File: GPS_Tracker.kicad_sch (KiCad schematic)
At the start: 46 parts, among them IC1 SX1278IMLTRT, IC2 PE4259, J8 Antena_Coaxial, Q1 2SC3356-T1B-A_AS, Y2 32MHz

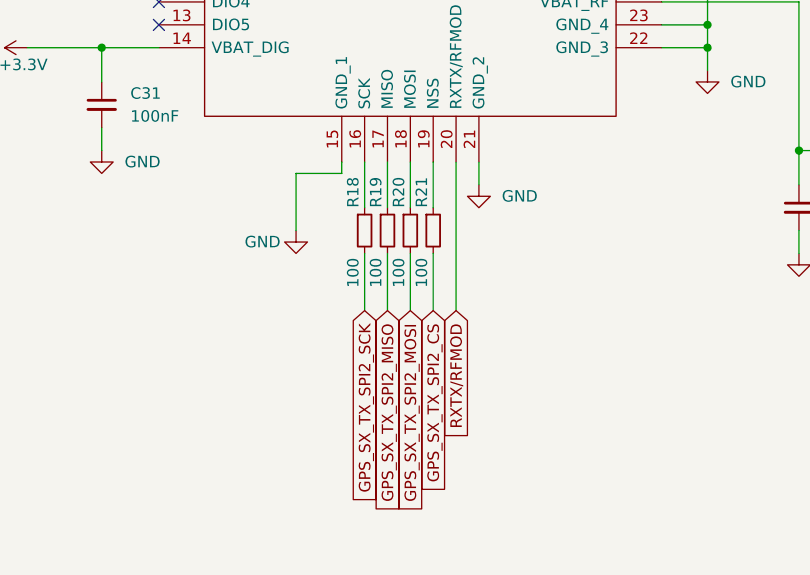
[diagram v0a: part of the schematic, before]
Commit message: Adding RF
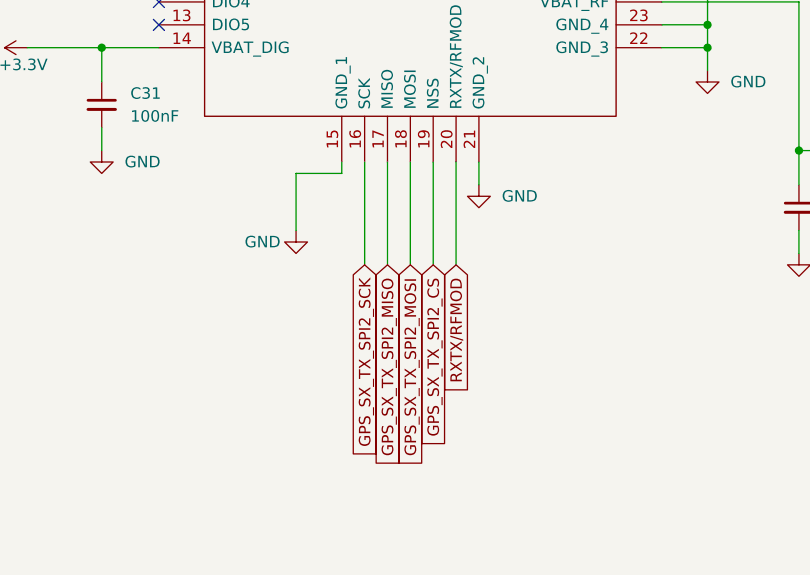
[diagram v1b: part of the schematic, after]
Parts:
- removed R18, R19, R20, R21: 100, Resistor_SMD:R_0402_1005Metric, symbol Device:R_Small
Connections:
- net GPS_SX_TX_SPI2_CS: now also IC1.19 (NSS)
- net GPS_SX_TX_SPI2_MISO: now also IC1.17 (MISO)
- net GPS_SX_TX_SPI2_MOSI: now also IC1.18 (MOSI)
- net GPS_SX_TX_SPI2_SCK: now also IC1.16 (SCK)
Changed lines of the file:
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@@
-    (stroke (width 0) (type default) (color 0 0 0 0))
-  )
-  (wire (pts (xy 100.965 127) (xy 100.965 132.08))
     (stroke (width 0) (type default) (color 0 0 0 0))
   )
@@
     (stroke (width 0) (type default) (color 0 0 0 0))
   )
-  (wire (pts (xy 95.885 127) (xy 95.885 132.08))
-    (stroke (width 0) (type default) (color 0 0 0 0))
-  )
   (wire (pts (xy 149.225 106.68) (xy 149.225 109.22))
     (stroke (width 0) (type default) (color 0 0 0 0))
@@
     (stroke (width 0) (type default) (color 0 0 0 0))
   )
-  (wire (pts (xy 100.965 137.16) (xy 100.965 143.51))
+  (wire (pts (xy 100.965 127) (xy 100.965 138.43))
     (stroke (width 0) (type default) (color 0 0 0 0))
   )
@@
     (stroke (width 0) (type default) (color 0 0 0 0))
   )
-  (wire (pts (xy 95.885 137.16) (xy 95.885 143.51))
+  (wire (pts (xy 95.885 127) (xy 95.885 138.43))
     (stroke (width 0) (type default) (color 0 0 0 0))
   )
@@
     (stroke (width 0) (type default) (color 0 0 0 0))
   )
-  (wire (pts (xy 103.505 127) (xy 103.505 132.08))
+  (wire (pts (xy 103.505 127) (xy 103.505 138.43))
     (stroke (width 0) (type default) (color 0 0 0 0))
   )
@@
     (stroke (width 0) (type default) (color 0 0 0 0))
   )
-  (wire (pts (xy 98.425 127) (xy 98.425 132.08))
+  (wire (pts (xy 98.425 127) (xy 98.425 138.43))
     (stroke (width 0) (type default) (color 0 0 0 0))
   )
@@
     (stroke (width 0) (type default) (color 0 0 0 0))
   )
-  (wire (pts (xy 103.505 137.16) (xy 103.505 143.51))
-    (stroke (width 0) (type default) (color 0 0 0 0))
-  )
   (wire (pts (xy 354.965 132.715) (xy 356.235 132.715))
     (stroke (width 0) (type default) (color 0 0 0 0))
   )
-  (wire (pts (xy 98.425 137.16) (xy 98.425 143.51))
-    (stroke (width 0) (type default) (color 0 0 0 0))
-  )
   (wire (pts (xy 56.515 55.88) (xy 51.435 55.88))
     (stroke (width 0) (type default) (color 0 0 0 0))
@@
     (stroke (width 0) (type default) (color 0 0 0 0))
   )
+  (wire (pts (xy 106.045 127) (xy 106.045 138.43))
+    (stroke (width 0) (type default) (color 0 0 0 0))
+  )
   (wire (pts (xy 250.825 97.79) (xy 225.425 97.79))
     (stroke (width 0) (type default) (color 0 0 0 0))
@@
     (stroke (width 0) (type default) (color 0 0 0 0))
   )
-  (wire (pts (xy 106.045 127) (xy 106.045 143.51))
-    (stroke (width 0) (type default) (color 0 0 0 0))
-  )
-  (global_label "GPS_SX_TX_SPI2_SCK" (shape input) (at 95.885 143.51 270) (fields_autoplaced)
+  (global_label "GPS_SX_TX_SPI2_SCK" (shape input) (at 95.885 138.43 270) (fields_autoplaced)
     (effects (font (size 1.27 1.27)) (justify right))
-    (property "Intersheet References" "${INTERSHEET_REFS}" (id 0) (at 95.8056 166.1826 90)
+    (property "Intersheet References" "${INTERSHEET_REFS}" (id 0) (at 95.8056 161.1026 90)
       (effects (font (size 1.27 1.27)) (justify right) hide)
     )
@@
     )
   )
-  (global_label "GPS_SX_TX_SPI2_MOSI" (shape input) (at 100.965 143.51 270) (fields_autoplaced)
+  (global_label "GPS_SX_TX_SPI2_MOSI" (shape input) (at 100.965 138.43 270) (fields_autoplaced)
     (effects (font (size 1.27 1.27)) (justify right))
-    (property "Intersheet References" "${INTERSHEET_REFS}" (id 0) (at 100.8856 167.0293 90)
+    (property "Intersheet References" "${INTERSHEET_REFS}" (id 0) (at 100.8856 161.9493 90)
       (effects (font (size 1.27 1.27)) (justify right) hide)
     )
@@
     )
   )
-  (global_label "GPS_SX_TX_SPI2_MISO" (shape input) (at 98.425 143.51 270) (fields_autoplaced)
+  (global_label "GPS_SX_TX_SPI2_MISO" (shape input) (at 98.425 138.43 270) (fields_autoplaced)
     (effects (font (size 1.27 1.27)) (justify right))
-    (property "Intersheet References" "${INTERSHEET_REFS}" (id 0) (at 98.3456 167.0293 90)
+    (property "Intersheet References" "${INTERSHEET_REFS}" (id 0) (at 98.3456 161.9493 90)
       (effects (font (size 1.27 1.27)) (justify right) hide)
     )
   )
-  (global_label "GPS_SX_TX_SPI2_CS" (shape input) (at 103.505 143.51 270) (fields_autoplaced)
+  (global_label "GPS_SX_TX_SPI2_CS" (shape input) (at 103.505 138.43 270) (fields_autoplaced)
     (effects (font (size 1.27 1.27)) (justify right))
-    (property "Intersheet References" "${INTERSHEET_REFS}" (id 0) (at 103.4256 164.9126 90)
+    (property "Intersheet References" "${INTERSHEET_REFS}" (id 0) (at 103.4256 159.8326 90)
       (effects (font (size 1.27 1.27)) (justify right) hide)
     )
@@
     )
   )
-  (global_label "RXTX{slash}RFMOD" (shape input) (at 106.045 143.51 270) (fields_autoplaced)
+  (global_label "RXTX{slash}RFMOD" (shape input) (at 106.045 138.43 270) (fields_autoplaced)
     (effects (font (size 1.27 1.27)) (justify right))
-    (property "Intersheet References" "${INTERSHEET_REFS}" (id 0) (at 105.9656 158.3207 90)
+    (property "Intersheet References" "${INTERSHEET_REFS}" (id 0) (at 105.9656 153.2407 90)
       (effects (font (size 1.27 1.27)) (justify right) hide)
     )
@@
     (pin "1")
   )
-  (symbol (lib_id "Device:R_Small") (at 100.965 134.62 0) (unit 1)
-    (in_bom yes) (on_board yes)
-    (property "Reference" "R20" (id 0) (at 99.695 132.08 90)
-      (effects (font (size 1.27 1.27)) (justify left))
-    )
-    (property "Value" "100" (id 1) (at 99.695 140.97 90)
-      (effects (font (size 1.27 1.27)) (justify left))
-    )
-    (property "Footprint" "Resistor_SMD:R_0402_1005Metric" (id 2) (at 100.965 134.62 0)
-      (effects (font (size 1.27 1.27)) hide)
-    )
-    (property "Datasheet" "~" (id 3) (at 100.965 134.62 0)
-      (effects (font (size 1.27 1.27)) hide)
-    )
-    (pin "1")
-    (pin "2")
-  )
   (symbol (lib_id "Device:C_Small") (at 186.055 97.79 90) (unit 1)
     (in_bom yes) (on_board yes)
@@
     )
     (property "Datasheet" "~" (id 3) (at 194.945 102.87 0)
-      (effects (font (size 1.27 1.27)) hide)
-    )
-    (pin "1")
-    (pin "2")
-  )
-  (symbol (lib_id "Device:R_Small") (at 95.885 134.62 0) (unit 1)
-    (in_bom yes) (on_board yes)
-    (property "Reference" "R18" (id 0) (at 94.615 132.08 90)
-      (effects (font (size 1.27 1.27)) (justify left))
-    )
-    (property "Value" "100" (id 1) (at 94.615 140.97 90)
-      (effects (font (size 1.27 1.27)) (justify left))
-    )
-    (property "Footprint" "Resistor_SMD:R_0402_1005Metric" (id 2) (at 95.885 134.62 0)
-      (effects (font (size 1.27 1.27)) hide)
-    )
-    (property "Datasheet" "~" (id 3) (at 95.885 134.62 0)
-      (effects (font (size 1.27 1.27)) hide)
-    )
-    (pin "1")
-    (pin "2")
-  )
-  (symbol (lib_id "Device:R_Small") (at 103.505 134.62 0) (unit 1)
-    (in_bom yes) (on_board yes)
-    (property "Reference" "R21" (id 0) (at 102.235 132.08 90)
-      (effects (font (size 1.27 1.27)) (justify left))
-    )
-    (property "Value" "100" (id 1) (at 102.235 140.97 90)
-      (effects (font (size 1.27 1.27)) (justify left))
-    )
-    (property "Footprint" "Resistor_SMD:R_0402_1005Metric" (id 2) (at 103.505 134.62 0)
-      (effects (font (size 1.27 1.27)) hide)
-    )
-    (property "Datasheet" "~" (id 3) (at 103.505 134.62 0)
       (effects (font (size 1.27 1.27)) hide)
     )
@@
     (pin "1")
   )
-  (symbol (lib_id "Device:R_Small") (at 98.425 134.62 0) (unit 1)
-    (in_bom yes) (on_board yes)
-    (property "Reference" "R19" (id 0) (at 97.155 132.08 90)
-      (effects (font (size 1.27 1.27)) (justify left))
-    )
-    (property "Value" "100" (id 1) (at 97.155 140.97 90)
-      (effects (font (size 1.27 1.27)) (justify left))
-    )
-    (property "Footprint" "Resistor_SMD:R_0402_1005Metric" (id 2) (at 98.425 134.62 0)
-      (effects (font (size 1.27 1.27)) hide)
-    )
-    (property "Datasheet" "~" (id 3) (at 98.425 134.62 0)
-      (effects (font (size 1.27 1.27)) hide)
-    )
-    (pin "1")
-    (pin "2")
-  )
   (symbol (lib_id "power:GND") (at 144.145 137.16 0) (unit 1)
